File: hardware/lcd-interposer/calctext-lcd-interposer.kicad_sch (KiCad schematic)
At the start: 10 parts, among them J1 HICENDA_FPC, J2 MAINBOARD_FFC

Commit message: Reorganize shared hardware libraries
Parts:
- J1: footprint calctext-lcd-interposer:Hirose_FH34SRJ-24S-0.5SH -> CalcText_Shared:Hirose_FH34SRJ-24S-0.5SH
- J2: footprint calctext-lcd-interposer:Hirose_FH34SRJ-10S-0.5SH -> CalcText_Shared:Hirose_FH34SRJ-10S-0.5SH
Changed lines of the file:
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@@
 			)
 		)
-		(property "Footprint" "calctext-lcd-interposer:Hirose_FH34SRJ-10S-0.5SH"
+		(property "Footprint" "CalcText_Shared:Hirose_FH34SRJ-10S-0.5SH"
 			(at 143.51 90.17 0)
 			(effects
@@
 			)
 		)
-		(property "Footprint" "calctext-lcd-interposer:Hirose_FH34SRJ-24S-0.5SH"
+		(property "Footprint" "CalcText_Shared:Hirose_FH34SRJ-24S-0.5SH"
 			(at 76.2 92.71 0)
 			(effects

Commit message: Refine hardware for fabrication and procurement
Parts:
- C1, C2, C3, C4, C5, C6, C7, C8: MPN (none) -> C1005X5R1E105K050BC; Manufacturer (none) -> TDK
- J1: value HICENDA_FPC -> FH34SRJ-24S-0.5SH; MPN (none) -> FH34SRJ-24S-0.5SH(99); Manufacturer (none) -> Hirose Electric
- J2: value MAINBOARD_FFC -> FH34SRJ-10S-0.5SH; MPN (none) -> FH34SRJ-10S-0.5SH(99); Manufacturer (none) -> Hirose Electric
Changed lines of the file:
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@@
 			)
 		)
-		(property "Datasheet" "~"
+		(property "Datasheet" "https://product.tdk.com/en/search/capacitor/ceramic/mlcc/info?part_no=C1005X5R1E105K050BC"
 			(at 140.97 124.46 0)
 			(effects
@@
 			)
 		)
-		(property "Description" "Unpolarized capacitor"
+		(property "Description" "1uF ±10%, 25V, X5R MLCC, 0402"
+			(at 140.97 124.46 0)
+			(effects
+				(font
+					(size 1.27 1.27)
+				)
+				(hide yes)
+			)
+		)
+		(property "MPN" "C1005X5R1E105K050BC"
+			(at 140.97 124.46 0)
+			(effects
+				(font
+					(size 1.27 1.27)
+				)
+				(hide yes)
+			)
+		)
+		(property "Manufacturer" "TDK"
 			(at 140.97 124.46 0)
 			(effects
@@
 			)
 		)
-		(property "Datasheet" "~"
+		(property "Datasheet" "https://product.tdk.com/en/search/capacitor/ceramic/mlcc/info?part_no=C1005X5R1E105K050BC"
 			(at 102.87 106.68 0)
 			(effects
@@
 			)
 		)
-		(property "Description" "Unpolarized capacitor"
+		(property "Description" "1uF ±10%, 25V, X5R MLCC, 0402"
+			(at 102.87 106.68 0)
+			(effects
+				(font
+					(size 1.27 1.27)
+				)
+				(hide yes)
+			)
+		)
+		(property "MPN" "C1005X5R1E105K050BC"
+			(at 102.87 106.68 0)
+			(effects
+				(font
+					(size 1.27 1.27)
+				)
+				(hide yes)
+			)
+		)
+		(property "Manufacturer" "TDK"
 			(at 102.87 106.68 0)
 			(effects
@@
 			)
 		)
-		(property "Datasheet" "~"
+		(property "Datasheet" "https://product.tdk.com/en/search/capacitor/ceramic/mlcc/info?part_no=C1005X5R1E105K050BC"
 			(at 128.27 124.46 0)
 			(effects
@@
 			)
 		)
-		(property "Description" "Unpolarized capacitor"
+		(property "Description" "1uF ±10%, 25V, X5R MLCC, 0402"
+			(at 128.27 124.46 0)
+			(effects
+				(font
+					(size 1.27 1.27)
+				)
+				(hide yes)
+			)
+		)
+		(property "MPN" "C1005X5R1E105K050BC"
+			(at 128.27 124.46 0)
+			(effects
+				(font
+					(size 1.27 1.27)
+				)
+				(hide yes)
+			)
+		)
+		(property "Manufacturer" "TDK"
 			(at 128.27 124.46 0)
 			(effects
@@
 			)
 		)
-		(property "Datasheet" "~"
+		(property "Datasheet" "https://product.tdk.com/en/search/capacitor/ceramic/mlcc/info?part_no=C1005X5R1E105K050BC"
 			(at 114.3 106.68 0)
 			(effects
@@
 			)
 		)
-		(property "Description" "Unpolarized capacitor"
+		(property "Description" "1uF ±10%, 25V, X5R MLCC, 0402"
+			(at 114.3 106.68 0)
+			(effects
+				(font
+					(size 1.27 1.27)
+				)
+				(hide yes)
+			)
+		)
+		(property "MPN" "C1005X5R1E105K050BC"
+			(at 114.3 106.68 0)
+			(effects
+				(font
+					(size 1.27 1.27)
+				)
+				(hide yes)
+			)
+		)
+		(property "Manufacturer" "TDK"
 			(at 114.3 106.68 0)
 			(effects
@@
 			)
 		)
-		(property "Datasheet" "~"
+		(property "Datasheet" "https://product.tdk.com/en/search/capacitor/ceramic/mlcc/info?part_no=C1005X5R1E105K050BC"
 			(at 102.87 81.28 0)
 			(effects
@@
 			)
 		)
-		(property "Description" "Unpolarized capacitor"
+		(property "Description" "1uF ±10%, 25V, X5R MLCC, 0402"
+			(at 102.87 81.28 0)
+			(effects
+				(font
+					(size 1.27 1.27)
+				)
+				(hide yes)
+			)
+		)
+		(property "MPN" "C1005X5R1E105K050BC"
+			(at 102.87 81.28 0)
+			(effects
+				(font
+					(size 1.27 1.27)
+				)
+				(hide yes)
+			)
+		)
+		(property "Manufacturer" "TDK"
 			(at 102.87 81.28 0)
 			(effects
@@
 			)
 		)
-		(property "Datasheet" "~"
+		(property "Datasheet" "https://product.tdk.com/en/search/capacitor/ceramic/mlcc/info?part_no=C1005X5R1E105K050BC"
 			(at 115.57 124.46 0)
 			(effects
@@
 			)
 		)
-		(property "Description" "Unpolarized capacitor"
+		(property "Description" "1uF ±10%, 25V, X5R MLCC, 0402"
+			(at 115.57 124.46 0)
+			(effects
+				(font
+					(size 1.27 1.27)
+				)
+				(hide yes)
+			)
+		)
+		(property "MPN" "C1005X5R1E105K050BC"
+			(at 115.57 124.46 0)
+			(effects
+				(font
+					(size 1.27 1.27)
+				)
+				(hide yes)
+			)
+		)
+		(property "Manufacturer" "TDK"
 			(at 115.57 124.46 0)
 			(effects
@@
 			)
 		)
-		(property "Datasheet" "~"
+		(property "Datasheet" "https://product.tdk.com/en/search/capacitor/ceramic/mlcc/info?part_no=C1005X5R1E105K050BC"
 			(at 153.67 124.46 0)
 			(effects
@@
 			)
 		)
-		(property "Description" "Unpolarized capacitor"
+		(property "Description" "1uF ±10%, 25V, X5R MLCC, 0402"
+			(at 153.67 124.46 0)
+			(effects
+				(font
+					(size 1.27 1.27)
+				)
+				(hide yes)
+			)
+		)
+		(property "MPN" "C1005X5R1E105K050BC"
+			(at 153.67 124.46 0)
+			(effects
+				(font
+					(size 1.27 1.27)
+				)
+				(hide yes)
+			)
+		)
+		(property "Manufacturer" "TDK"
 			(at 153.67 124.46 0)
 			(effects
@@
 			)
 		)
-		(property "Datasheet" "~"
+		(property "Datasheet" "https://product.tdk.com/en/search/capacitor/ceramic/mlcc/info?part_no=C1005X5R1E105K050BC"
 			(at 102.87 124.46 0)
 			(effects
@@
 			)
 		)
-		(property "Description" "Unpolarized capacitor"
+		(property "Description" "1uF ±10%, 25V, X5R MLCC, 0402"
+			(at 102.87 124.46 0)
+			(effects
+				(font
+					(size 1.27 1.27)
+				)
+				(hide yes)
+			)
+		)
+		(property "MPN" "C1005X5R1E105K050BC"
+			(at 102.87 124.46 0)
+			(effects
+				(font
+					(size 1.27 1.27)
+				)
+				(hide yes)
+			)
+		)
+		(property "Manufacturer" "TDK"
 			(at 102.87 124.46 0)
 			(effects
@@
 			)
 		)
-		(property "Value" "MAINBOARD_FFC"
+		(property "Value" "FH34SRJ-10S-0.5SH"
 			(at 146.05 92.7099 0)
 			(effects
@@
 			)
 		)
-		(property "Datasheet" "~"
+		(property "Datasheet" "https://www.hirose.com/en/product/document?clcode=CL0580-1251-5-99&productname=FH34SRJ-10S-0.5SH(99)&series=FH34SRJ&documenttype=SpecSheet&lang=en&documentid=0000414526"
 			(at 143.51 90.17 0)
 			(effects
@@
 			)
 		)
-		(property "Description" "Generic connector, single row, 01x10, script generated (kicad-library-utils/schlib/autogen/connector/)"
+		(property "Description" "10-position 0.5 mm pitch back-flip ZIF FFC/FPC receptacle, 1.0 mm height, for 0.3 mm FFC/FPC"
+			(at 143.51 90.17 0)
+			(effects
+				(font
+					(size 1.27 1.27)
+				)
+				(hide yes)
+			)
+		)
+		(property "MPN" "FH34SRJ-10S-0.5SH(99)"
+			(at 143.51 90.17 0)
+			(effects
+				(font
+					(size 1.27 1.27)
+				)
+				(hide yes)
+			)
+		)
+		(property "Manufacturer" "Hirose Electric"
 			(at 143.51 90.17 0)
 			(effects
@@
 			)
 		)
-		(property "Value" "HICENDA_FPC"
+		(property "Value" "FH34SRJ-24S-0.5SH"
 			(at 73.66 95.2499 0)
 			(effects
@@
 			)
 		)
-		(property "Datasheet" "~"
+		(property "Datasheet" "https://www.hirose.com/en/product/document?clcode=CL0580-1255-6-99&productname=FH34SRJ-24S-0.5SH(99)&series=FH34SRJ&documenttype=SpecSheet&lang=en&documentid=0000414526"
 			(at 76.2 92.71 0)
 			(effects
@@
 			)
 		)
-		(property "Description" "Generic connector, single row, 01x24, script generated (kicad-library-utils/schlib/autogen/connector/)"
+		(property "Description" "24-position 0.5 mm pitch ZIF FFC/FPC receptacle, 1.0 mm height, for 0.3 mm FFC/FPC"
 			(at 76.2 92.71 0)
 			(effects
+				(font
+					(size 1.27 1.27)
+				)
+				(hide yes)
+			)
+		)
+		(property "MPN" "FH34SRJ-24S-0.5SH(99)"
+			(at 76.2 92.71 0)
+			(effects
+				(font
+					(size 1.27 1.27)
+				)
+				(hide yes)
+			)
+		)
+		(property "Manufacturer" "Hirose Electric"
+			(at 76.2 92.71 0)
+			(effects

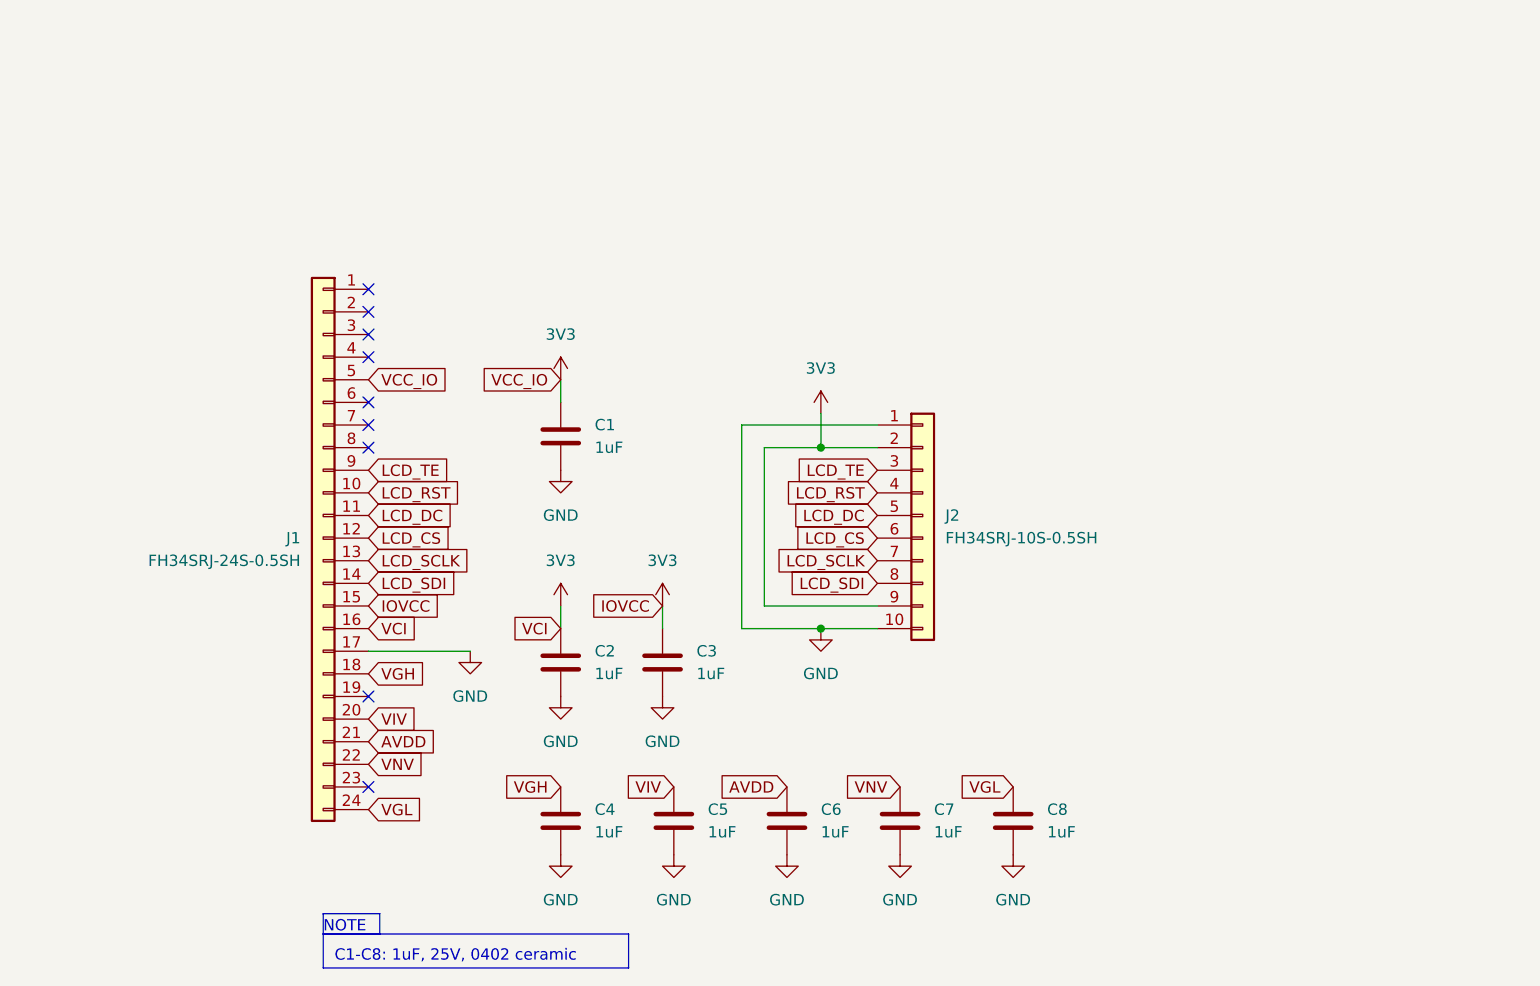
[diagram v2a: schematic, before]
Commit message: Finalise hardware sanity-check cleanup
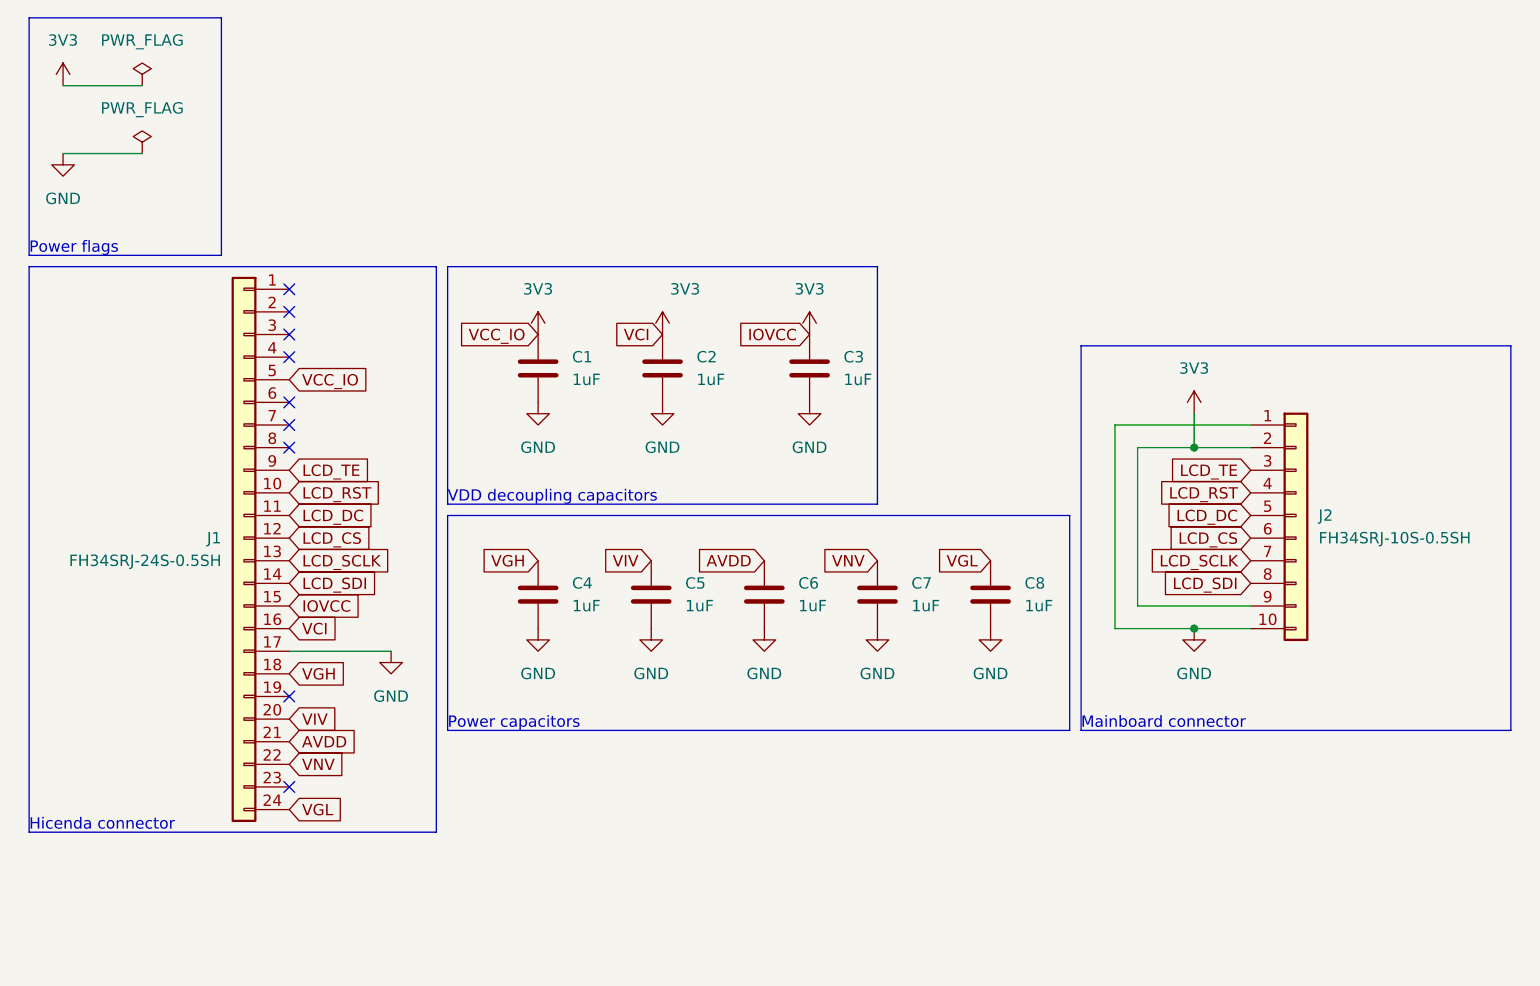
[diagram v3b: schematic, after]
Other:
- note added: "Hicenda connector"
- note added: "Mainboard connector"
- note added: "Power capacitors"
- note added: "Power flags"
- note added: "VDD decoupling capacitors"
- note removed: "C1-C8: 1uF, 25V, 0402 ceramic"
- note removed: "NOTE"
- moved on the sheet: C1, C2, C3, C4, C5, C6, C7, C8, J1, J2
